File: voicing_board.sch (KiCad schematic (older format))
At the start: 274 parts, among them Q1 MMBT3904, Q14 MMBT3904, Q15 MMBT3904, Q16 MMBT3904, Q17 MMBT3904, Q18 MMBT3904, Q19 MMBT3904, Q2 MMBT3904, Q20 MMBT3904, Q21 MMBT3904, Q22/23 DMMT3904W, Q24 MMBT3904, Q25 MMBT3904, Q26 MMBT3904, Q27 MMBT3904, Q28-1 MMBT3904, Q29-1 MMBT3904, Q3 MMBT3904, Q30 MMBT3904, Q31-1 MMBT3904, Q4 MMBT3904, Q5 MMBT3906, Q6 MMBT3906, Q7 MMBT3906, Q8 MMBT3906, Q9 MMBT3904, U1 MC14584, U2 4558, U3 4558, U5 4558, U6-1 4558, U7 4558

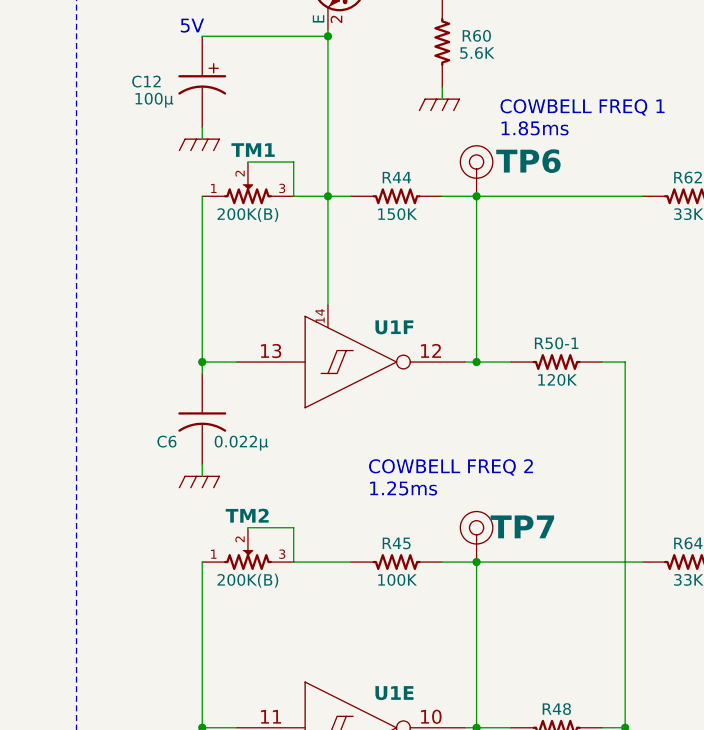
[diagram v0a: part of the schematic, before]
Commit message: removed incorrect junction between R44, TM1 and  pin 14 of U1F, disconnected  pin 3 of TM1 and TM2
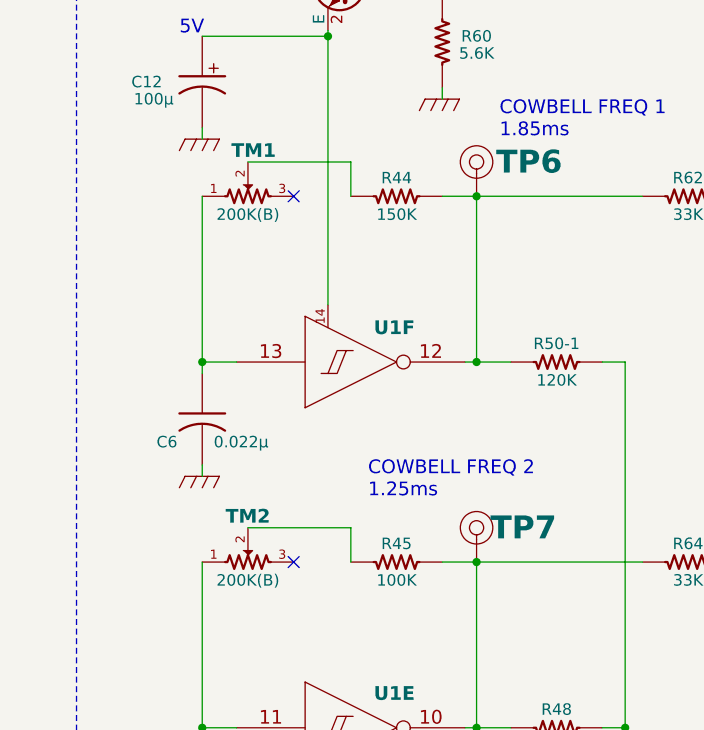
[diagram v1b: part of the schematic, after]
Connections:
- wire segments 519 -> 517
- no-connect marks 0 -> 2
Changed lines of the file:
@@
 Connection ~ 1750 6175
 Wire Wire Line
-	1400 6725 1600 6725
-Wire Wire Line
-	1600 6725 1600 6875
-Wire Wire Line
-	1600 6875 1850 6875
-Connection ~ 1750 6875
+	1400 6725 1850 6725
 Wire Wire Line
 	1200 6875 1200 7650
@@
 Connection ~ 1200 7600
 Wire Wire Line
-	1600 8325 1600 8475
-Wire Wire Line
 	1200 8475 1200 9250
 Wire Wire Line
@@
 Connection ~ 1200 9200
 Wire Wire Line
-	1600 8325 1400 8325
-Wire Wire Line
-	1600 8475 1850 8475
+	1400 8325 1850 8325
 Wire Wire Line
 	2950 7600 3050 7600
@@
 Connection ~ 13350 9025
 Connection ~ 19150 5850
+NoConn ~ 1600 6875
+Wire Wire Line
+	1850 6725 1850 6875
+Wire Wire Line
+	1850 8325 1850 8475
+NoConn ~ 1600 8475
 $EndSCHEMATC

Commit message: done. should probably label some test points though. about to do footprint checking
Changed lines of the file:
@@
 Wire Wire Line
 	6225 14250 7075 14250
-Connection ~ 5250 12725
 Wire Wire Line
 	5250 12725 5250 14450

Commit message: updates to schematic with build notes
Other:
- note added: "Change R60 to 7.5K\nfor 5V at Q9 emitter"
- note added: "Increase C41 to \naccommodate 1meg pot\nisntead of 2meg pot?"
- note added: "Increase C60-1 to compensate\nfor 1meg decay pot instead of 2meg?"
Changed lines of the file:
@@
 	1850 8325 1850 8475
 NoConn ~ 1600 8475
+Text Notes 2475 6300 0    60   ~ 0
+Change R60 to 7.5K\nfor 5V at Q9 emitter
+Text Notes 9675 12925 0    60   ~ 0
+Increase C41 to \naccommodate 1meg pot\nisntead of 2meg pot?
+Text Notes 9575 4850 0    60   ~ 0
+Increase C60-1 to compensate\nfor 1meg decay pot instead of 2meg?
 $EndSCHEMATC

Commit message: started version 2.0 schematic changes. Added missing R365, replaced LM13700 VCA with discrete BA662 from Open Music Labs, replaced clap and hi hat matched pairs with single NPN/PNP Qs
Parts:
- removed Q22/23: DMMT3904W, MyModules:SOT363-JRL, symbol DMMT3904W
- added Q22, Q23: MMBT3904, MyModules:SOT23-132-JRL, symbol MMBT3904

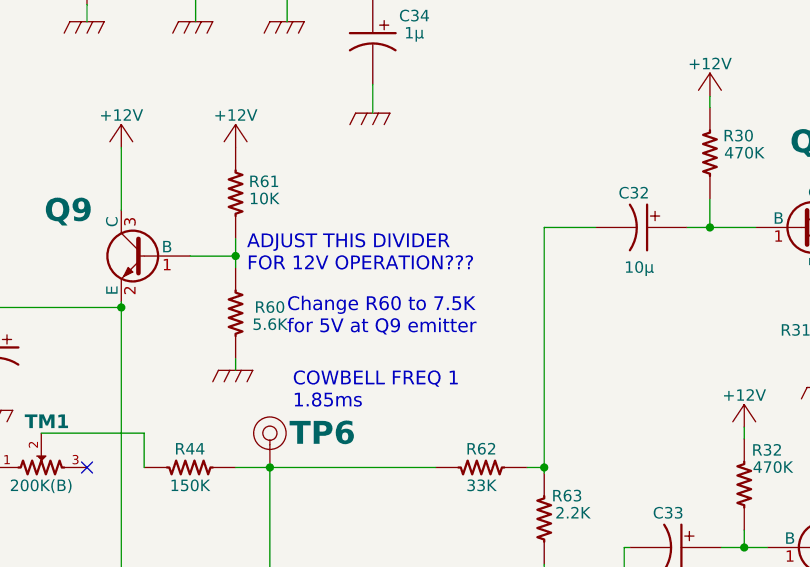
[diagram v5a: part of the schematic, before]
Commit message: Sync LED control pins added, tom clipping diodes changed to BAT54 with series resistor
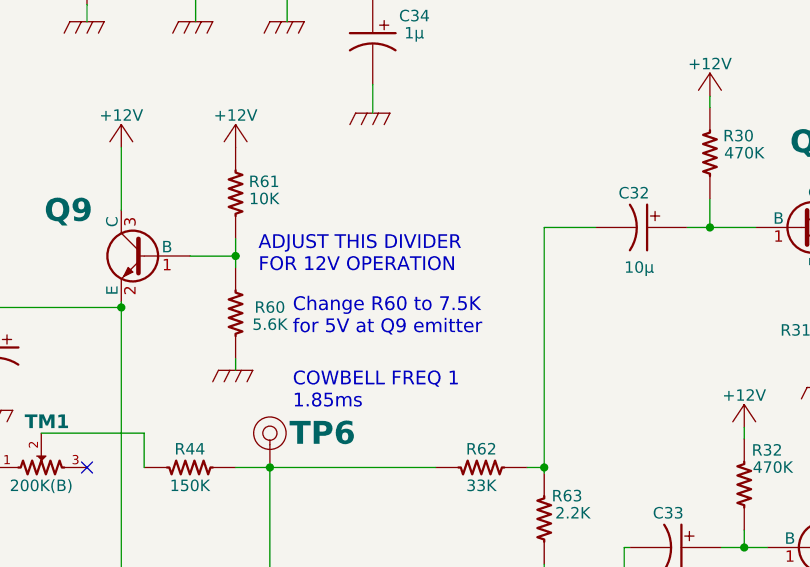
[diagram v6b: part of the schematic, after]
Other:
- note added: "ADJUST THIS DIVIDER\nFOR 12V OPERATION\n\n"
- note removed: "ADJUST THIS DIVIDER\nFOR 12V OPERATION???"
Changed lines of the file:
@@
 	1    0    0    -1
 $EndComp
-Text Notes 2300 6025 0    60   ~ 0
-ADJUST THIS DIVIDER\nFOR 12V OPERATION???
 $Comp
 L TL072- U6-1
@@
 	1850 8325 1850 8475
 NoConn ~ 1600 8475
-Text Notes 2475 6300 0    60   ~ 0
+Text Notes 2500 6300 0    60   ~ 0
 Change R60 to 7.5K\nfor 5V at Q9 emitter
 Text Notes 9675 12925 0    60   ~ 0
@@
 	-1   0    0    -1
 $EndComp
+Text Notes 2350 6125 0    60   ~ 0
+ADJUST THIS DIVIDER\nFOR 12V OPERATION\n\n
 $EndSCHEMATC

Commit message: assigning footprints before importing updated netlist into pcbnew
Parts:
- TM1, TM2: footprint MyModules:Bourns_3362P -> MyModules:TC33X-2

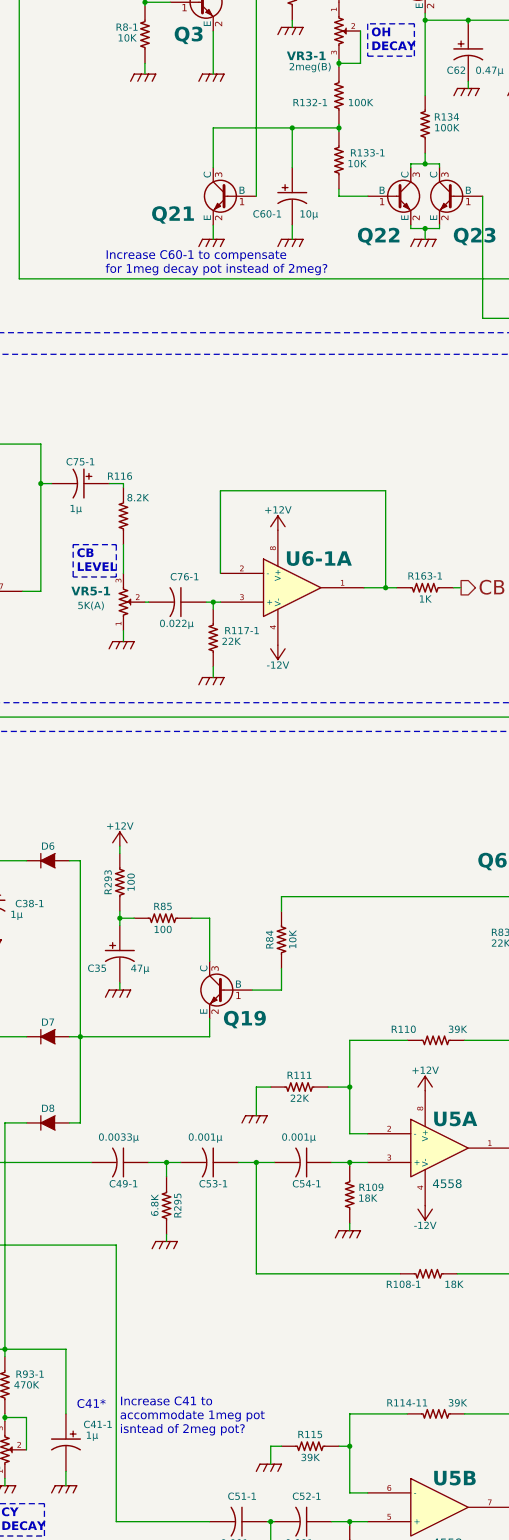
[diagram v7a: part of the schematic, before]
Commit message: surface mount polarized capacitors replace through hole capaictors. Updated netlist not yet imported into pcbnew
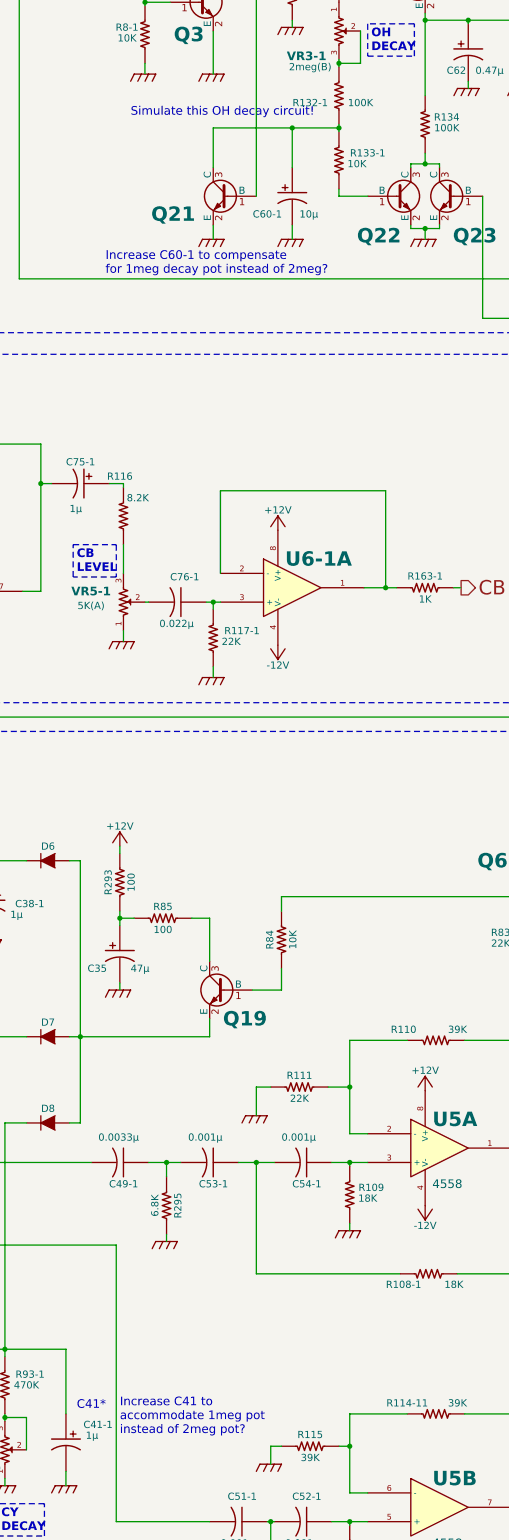
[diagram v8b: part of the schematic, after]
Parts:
- C12, C35, C61-1: footprint MyModules:2MM-POL-CAP -> Capacitors_SMD:c_elec_6.3x5.3
- C32, C33, C34, C37, C38-1, C39-1, C40-1, C41-1, C45-1, C60-1, C62, C63-1, C75-1, C9: footprint MyModules:2MM-POL-CAP -> Capacitors_SMD:c_elec_4x5.3
- C78-1, C8-1, C83-1: footprint MyModules:2MM-POL-CAP -> Capacitors_SMD:c_elec_5x5.3
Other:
- note added: "Increase C41 to \naccommodate 1meg pot\ninstead of 2meg pot?"
- note added: "Simulate this OH decay circuit!"
- note removed: "Increase C41 to \naccommodate 1meg pot\nisntead of 2meg pot?"
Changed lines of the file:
@@
 F 0 "C12" H 1375 6375 50  0000 L CNN
 F 1 "100μ" H 1325 6300 50  0000 L CNN
-F 2 "MyModules:2MM-POL-CAP" H 1200 6375 60  0001 C CNN
+F 2 "Capacitors_SMD:c_elec_6.3x5.3" H 1200 6375 60  0001 C CNN
 F 3 "" H 1200 6375 60  0000 C CNN
 	1    1200 6375
@@
 F 0 "C32" V 3875 5725 50  0000 L CNN
 F 1 "10μ" V 4200 5750 50  0000 L CNN
-F 2 "MyModules:2MM-POL-CAP" H 4025 5825 60  0001 C CNN
+F 2 "Capacitors_SMD:c_elec_4x5.3" H 4025 5825 60  0001 C CNN
 F 3 "" H 4025 5825 60  0000 C CNN
 	1    4025 5825
@@
 F 0 "C33" V 4025 7125 50  0000 L CNN
 F 1 "10μ" V 4350 7150 50  0000 L CNN
-F 2 "MyModules:2MM-POL-CAP" H 4175 7225 60  0001 C CNN
+F 2 "Capacitors_SMD:c_elec_4x5.3" H 4175 7225 60  0001 C CNN
 F 3 "" H 4175 7225 60  0000 C CNN
 	1    4175 7225
@@
 F 0 "C75-1" V 9250 6200 50  0000 L CNN
 F 1 "1μ" V 9575 6225 50  0000 L CNN
-F 2 "MyModules:2MM-POL-CAP" H 9400 6300 60  0001 C CNN
+F 2 "Capacitors_SMD:c_elec_4x5.3" H 9400 6300 60  0001 C CNN
 F 3 "" H 9400 6300 60  0000 C CNN
 	1    9400 6300
@@
 F 0 "C9" H 2600 4550 50  0000 L CNN
 F 1 "0.47μ" H 2525 4475 50  0000 L CNN
-F 2 "MyModules:2MM-POL-CAP" H 2475 4600 60  0001 C CNN
+F 2 "Capacitors_SMD:c_elec_4x5.3" H 2475 4600 60  0001 C CNN
 F 3 "" H 2475 4600 60  0000 C CNN
 	1    2475 4600
@@
 F 0 "C34" H 2600 5100 50  0000 L CNN
 F 1 "1μ" H 2625 5025 50  0000 L CNN
-F 2 "MyModules:2MM-POL-CAP" H 2850 5000 60  0001 C CNN
+F 2 "Capacitors_SMD:c_elec_4x5.3" H 2850 5000 60  0001 C CNN
 F 3 "" H 2850 5000 60  0000 C CNN
 	1    2850 5000
@@
 F 0 "C40-1" H 8500 10400 50  0000 L CNN
 F 1 "1μ" H 8225 10400 50  0000 L CNN
-F 2 "MyModules:2MM-POL-CAP" H 8425 10500 60  0001 C CNN
+F 2 "Capacitors_SMD:c_elec_4x5.3" H 8425 10500 60  0001 C CNN
 F 3 "" H 8425 10500 60  0000 C CNN
 	1    8425 10500
@@
 F 0 "C38-1" H 8400 9225 50  0000 L CNN
 F 1 "1μ" H 8550 9150 50  0000 L CNN
-F 2 "MyModules:2MM-POL-CAP" H 8775 9225 60  0001 C CNN
+F 2 "Capacitors_SMD:c_elec_4x5.3" H 8775 9225 60  0001 C CNN
 F 3 "" H 8775 9225 60  0000 C CNN
 	1    8775 9225
@@
 F 0 "C39-1" H 6725 10950 50  0000 L CNN
 F 1 "0.47μ" H 6825 10800 50  0000 L CNN
-F 2 "MyModules:2MM-POL-CAP" H 7100 10925 60  0001 C CNN
+F 2 "Capacitors_SMD:c_elec_4x5.3" H 7100 10925 60  0001 C CNN
 F 3 "" H 7100 10925 60  0000 C CNN
 	1    7100 10925
@@
 F 0 "C37" H 8500 9575 50  0000 L CNN
 F 1 "2.2μ" H 8175 9575 50  0000 L CNN
-F 2 "MyModules:2MM-POL-CAP" H 8425 9675 60  0001 C CNN
+F 2 "Capacitors_SMD:c_elec_4x5.3" H 8425 9675 60  0001 C CNN
 F 3 "" H 8425 9675 60  0000 C CNN
 	1    8425 9675
@@
 F 0 "C35" H 9450 9475 50  0000 L CNN
 F 1 "47μ" H 9750 9475 50  0000 L CNN
-F 2 "MyModules:2MM-POL-CAP" H 9675 9575 60  0001 C CNN
+F 2 "Capacitors_SMD:c_elec_6.3x5.3" H 9675 9575 60  0001 C CNN
 F 3 "" H 9675 9575 60  0000 C CNN
 	1    9675 9575
@@
 F 0 "C41-1" H 8975 13100 50  0000 L CNN
 F 1 "1μ" H 9075 13025 50  0000 L CNN
-F 2 "MyModules:2MM-POL-CAP" H 9300 12975 60  0001 C CNN
+F 2 "Capacitors_SMD:c_elec_4x5.3" H 9300 12975 60  0001 C CNN
 F 3 "" H 9300 12975 60  0000 C CNN
 	1    9300 12975
@@
 F 0 "C45-1" H 6625 13725 50  0000 L CNN
 F 1 "2.2μ" H 7050 13725 50  0000 L CNN
-F 2 "MyModules:2MM-POL-CAP" H 6975 13625 60  0001 C CNN
+F 2 "Capacitors_SMD:c_elec_4x5.3" H 6975 13625 60  0001 C CNN
 F 3 "" H 6975 13625 60  0000 C CNN
 	1    6975 13625
@@
 F 0 "C78-1" V 14800 10900 50  0000 L CNN
 F 1 "33μ" V 15025 10775 50  0000 L CNN
-F 2 "MyModules:2MM-POL-CAP" H 14950 11000 60  0001 C CNN
+F 2 "Capacitors_SMD:c_elec_5x5.3" H 14950 11000 60  0001 C CNN
 F 3 "" H 14950 11000 60  0000 C CNN
 	1    14950 11000
@@
 F 0 "C60-1" H 10600 4175 50  0000 L CNN
 F 1 "10μ" H 10925 4175 50  0000 L CNN
-F 2 "MyModules:2MM-POL-CAP" H 10875 4300 60  0001 C CNN
+F 2 "Capacitors_SMD:c_elec_4x5.3" H 10875 4300 60  0001 C CNN
 F 3 "" H 10875 4300 60  0000 C CNN
 	1    10875 4300
@@
 F 0 "C62" H 11950 3175 50  0000 L CNN
 F 1 "0.47μ" H 12150 3175 50  0000 L CNN
-F 2 "MyModules:2MM-POL-CAP" H 12100 3300 60  0001 C CNN
+F 2 "Capacitors_SMD:c_elec_4x5.3" H 12100 3300 60  0001 C CNN
 F 3 "" H 12100 3300 60  0000 C CNN
 	1    12100 3300
@@
 F 0 "C61-1" H 13175 2575 50  0000 L CNN
 F 1 "47μ" H 13175 2500 50  0000 L CNN
-F 2 "MyModules:2MM-POL-CAP" H 13050 2550 60  0001 C CNN
+F 2 "Capacitors_SMD:c_elec_6.3x5.3" H 13050 2550 60  0001 C CNN
 F 3 "" H 13050 2550 60  0000 C CNN
 	1    13050 2550
@@
 F 0 "C63-1" H 13800 5325 50  0000 L CNN
 F 1 "0.47μ" H 13800 5250 50  0000 L CNN
-F 2 "MyModules:2MM-POL-CAP" H 13700 5375 60  0001 C CNN
+F 2 "Capacitors_SMD:c_elec_4x5.3" H 13700 5375 60  0001 C CNN
 F 3 "" H 13700 5375 60  0000 C CNN
 	1    13700 5375
@@
 F 0 "C83-1" V 19325 4400 50  0000 L CNN
 F 1 "33μ" V 19525 4400 50  0000 L CNN
-F 2 "MyModules:2MM-POL-CAP" H 19450 4625 60  0001 C CNN
+F 2 "Capacitors_SMD:c_elec_5x5.3" H 19450 4625 60  0001 C CNN
 F 3 "" H 19450 4625 60  0000 C CNN
 	1    19450 4625
@@
 F 0 "C8-1" V 19375 2175 50  0000 L CNN
 F 1 "33μ" V 19500 2225 50  0000 L CNN
-F 2 "MyModules:2MM-POL-CAP" H 19450 2450 60  0001 C CNN
+F 2 "Capacitors_SMD:c_elec_5x5.3" H 19450 2450 60  0001 C CNN
 F 3 "" H 19450 2450 60  0000 C CNN
 	1    19450 2450
@@
 Change R60 to 7.5K\nfor 5V at Q9 emitter
 Text Notes 9675 12925 0    60   ~ 0
-Increase C41 to \naccommodate 1meg pot\nisntead of 2meg pot?
+Increase C41 to \naccommodate 1meg pot\ninstead of 2meg pot?
 Text Notes 9575 4850 0    60   ~ 0
 Increase C60-1 to compensate\nfor 1meg decay pot instead of 2meg?
@@
 Text Notes 2350 6125 0    60   ~ 0
 ADJUST THIS DIVIDER\nFOR 12V OPERATION\n\n
+Text Notes 9750 3750 0    60   ~ 0
+Simulate this OH decay circuit!
 $EndSCHEMATC
